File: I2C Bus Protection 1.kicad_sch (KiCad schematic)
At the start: 18 parts, among them Q1 NX3008NBKS, Q2 MBT2222ADW1T1, Q3 NX3008NBKS, Q4 MBT2222ADW1T1

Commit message: Layout mostly complete
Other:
- title: (none) -> Argus Reaction Wheel
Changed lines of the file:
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@@
 	(generator_version "8.0")
 	(paper "A4")
+	(title_block
+		(title "Argus Reaction Wheel")
+		(date "2025-03-24")
+		(rev "1.0")
+	)
 	(junction
 		(at 87.63 78.74)

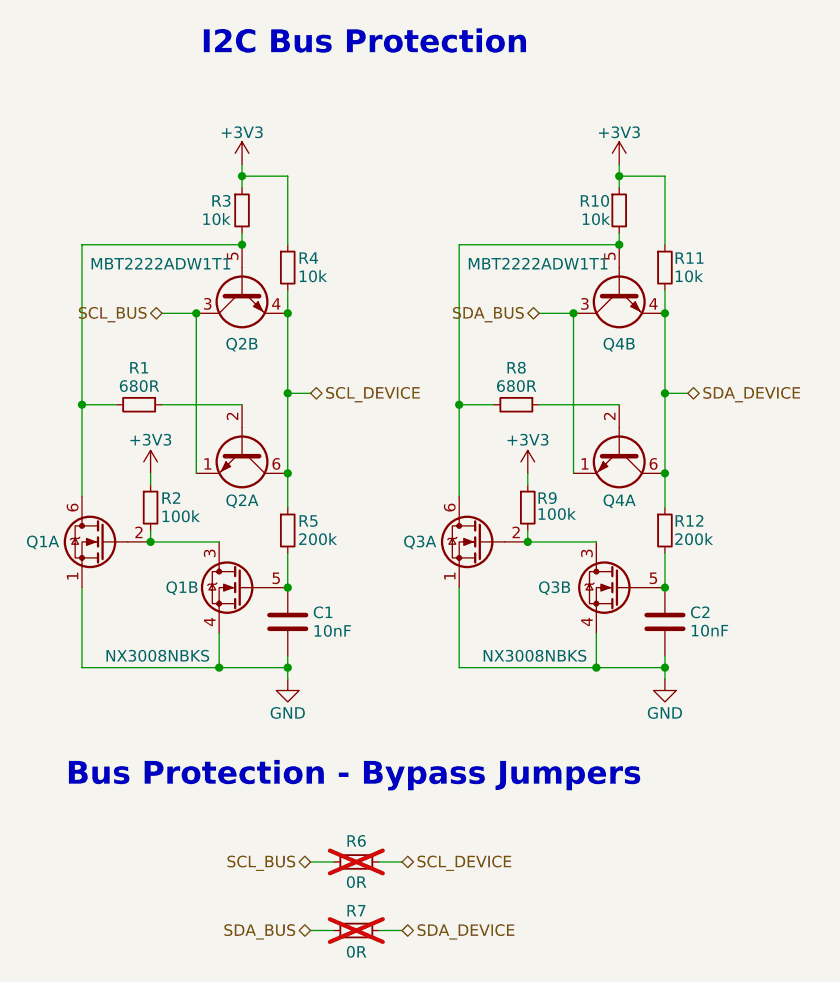
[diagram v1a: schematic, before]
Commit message: Add and correct BOM for easy Digikey ordering
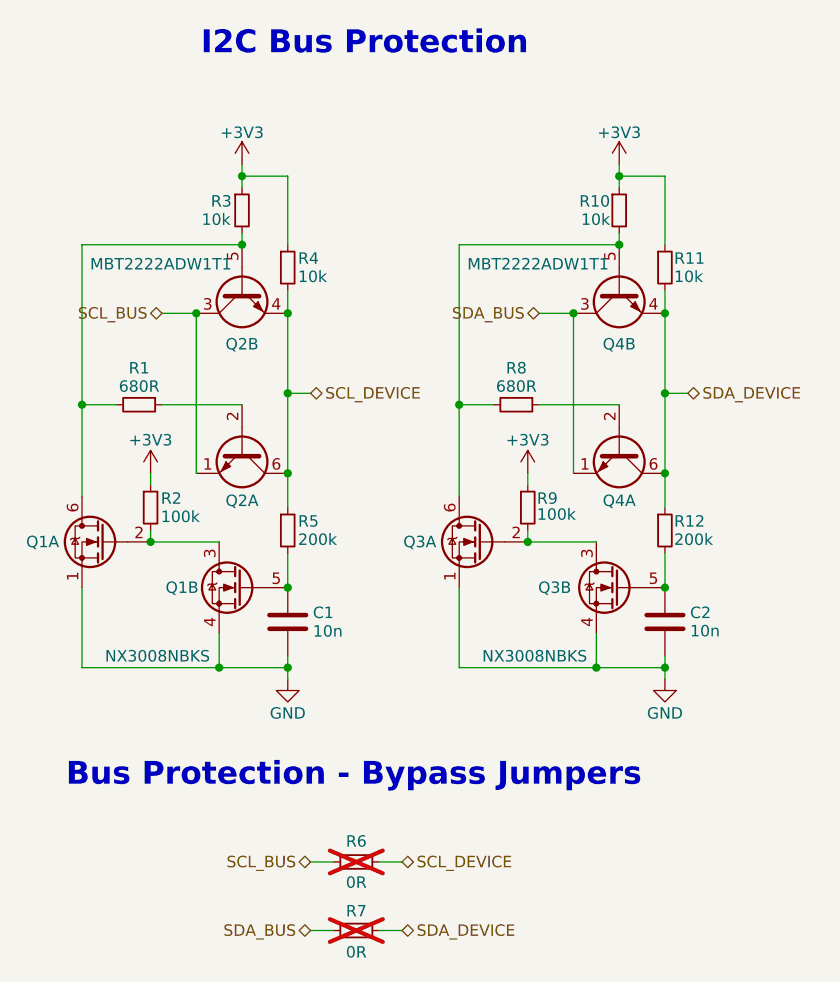
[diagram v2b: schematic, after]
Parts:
- C1, C2: value 10nF -> 10n; Digikey (none) -> https://www.digikey.com/en/products/detail/samsung-electro-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; Digikey PN (none) -> 490-4934-1-ND; MPN (none) -> CL10B103KO8WPNC; Part (none) -> CL10B103KO8WPNC
- Q1, Q3: Digikey (none) -> https://www.digikey.com/en/products/detail/nexperia-usa-inc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; Digikey PN (none) -> 1727-1221-1-ND; MPN (none) -> NX3008NBKS,115; Part (none) -> NX3008NBKS,115
- Q2, Q4: Digikey (none) -> https://www.digikey.com/en/products/detail/onsemi/MBT2222AD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; Digikey PN (none) -> MBT2222ADW1T1GOSCT-ND; MPN (none) -> MBT2222ADW1T1G; Part (none) -> MBT2222ADW1T1G
- R1, R8: Digikey (none) -> https://www.digikey.com/en/products/detail/yageo/RC0603FR-0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; Digikey PN (none) -> 311-680HRCT-ND; MPN (none) -> RC0603FR-07680RL; Part (none) -> RC0603FR-07680RL
- R10, R11, R3, R4: Digikey (none) -> https://www.digikey.com/en/products/detail/yageo/RC0603FR-0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; Digikey PN (none) -> 311-10.0KHRCT-ND; MPN (none) -> RC0603FR-0710KL; Part (none) -> RC0603FR-0710KL
- R12, R5: Digikey (none) -> https://www.digikey.com/en/products/detail/yageo/RC0603FR-0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; Digikey PN (none) -> 311-200KHRCT-ND; MPN (none) -> RC0603FR-07200KL; Part (none) -> RC0603FR-07200KL
- R2, R9: Digikey (none) -> https://www.digikey.com/en/products/detail/yageo/RC0603FR-0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; Digikey PN (none) -> 311-100KHRCT-ND; MPN (none) -> RC0603FR-07100KL; Part (none) -> RC0603FR-07100KL
- R6, R7: Digikey (none) -> https://www.digikey.com/en/products/detail/bourns-inc/CR060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; Digikey PN (none) -> CR0603-J/-000ELFCT-ND; MPN (none) -> CR0603-J/-000ELF; Part (none) -> CR0603-J/-000ELF
